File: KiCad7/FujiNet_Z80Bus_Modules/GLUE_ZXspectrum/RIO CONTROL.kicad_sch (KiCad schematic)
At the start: 8 parts, among them IC1 74HC32N, IC2 7404N, IC4 74HC08N, IC8 74HC32N, IC9 74HC08N, U1 74HC244N

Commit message: Reorganised the project again
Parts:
- renumbered U1 to U?
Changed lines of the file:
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@@
         )
         (path "/532c0392-800e-45cc-8170-6d32f2390e83/6a1fd481-1635-4a64-b244-c204161ad407/470a76e9-5ba5-4732-b286-3d7fc5c85df9"
-          (reference "IC8") (unit 2)
+          (reference "IC?") (unit 2)
         )
       )
@@
         )
         (path "/532c0392-800e-45cc-8170-6d32f2390e83/6a1fd481-1635-4a64-b244-c204161ad407/470a76e9-5ba5-4732-b286-3d7fc5c85df9"
-          (reference "IC5") (unit 2)
+          (reference "IC?") (unit 2)
         )
       )
@@
         )
         (path "/532c0392-800e-45cc-8170-6d32f2390e83/6a1fd481-1635-4a64-b244-c204161ad407/470a76e9-5ba5-4732-b286-3d7fc5c85df9"
-          (reference "#PWR064") (unit 1)
+          (reference "#PWR?") (unit 1)
         )
       )
@@
         )
         (path "/532c0392-800e-45cc-8170-6d32f2390e83/6a1fd481-1635-4a64-b244-c204161ad407/470a76e9-5ba5-4732-b286-3d7fc5c85df9"
-          (reference "IC11") (unit 5)
+          (reference "IC?") (unit 5)
         )
       )
@@
         )
         (path "/532c0392-800e-45cc-8170-6d32f2390e83/6a1fd481-1635-4a64-b244-c204161ad407/470a76e9-5ba5-4732-b286-3d7fc5c85df9"
-          (reference "IC7") (unit 1)
+          (reference "IC?") (unit 1)
         )
       )
@@
         )
         (path "/532c0392-800e-45cc-8170-6d32f2390e83/6a1fd481-1635-4a64-b244-c204161ad407/470a76e9-5ba5-4732-b286-3d7fc5c85df9"
-          (reference "IC8") (unit 1)
+          (reference "IC?") (unit 1)
         )
       )
@@
         )
         (path "/532c0392-800e-45cc-8170-6d32f2390e83/6a1fd481-1635-4a64-b244-c204161ad407/470a76e9-5ba5-4732-b286-3d7fc5c85df9"
-          (reference "IC8") (unit 3)
+          (reference "IC?") (unit 3)
         )
       )
@@
   (symbol (lib_id "power:GND") (at 214.63 152.4 0) (unit 1)
     (in_bom yes) (on_board yes) (dnp no) (fields_autoplaced)
-    (property "Reference" "#PWR065" (at 214.63 158.75 0)
+    (property "Reference" "#PWR?" (at 214.63 158.75 0)
       (effects (font (size 1.27 1.27)) hide)
     )
@@
       (project "FujiNet_Z80Bus_ReferenceDesign"
         (path "/532c0392-800e-45cc-8170-6d32f2390e83/6a1fd481-1635-4a64-b244-c204161ad407/470a76e9-5ba5-4732-b286-3d7fc5c85df9"
-          (reference "#PWR065") (unit 1)
+          (reference "#PWR?") (unit 1)
         )
       )
@@
         )
         (path "/532c0392-800e-45cc-8170-6d32f2390e83/6a1fd481-1635-4a64-b244-c204161ad407/470a76e9-5ba5-4732-b286-3d7fc5c85df9"
-          (reference "#PWR066") (unit 1)
+          (reference "#PWR?") (unit 1)
         )
       )
@@
         )
         (path "/532c0392-800e-45cc-8170-6d32f2390e83/6a1fd481-1635-4a64-b244-c204161ad407/470a76e9-5ba5-4732-b286-3d7fc5c85df9"
-          (reference "IC7") (unit 2)
+          (reference "IC?") (unit 2)
         )
       )
@@
         )
         (path "/532c0392-800e-45cc-8170-6d32f2390e83/6a1fd481-1635-4a64-b244-c204161ad407/470a76e9-5ba5-4732-b286-3d7fc5c85df9"
-          (reference "IC12") (unit 3)
+          (reference "IC?") (unit 3)
         )
       )
@@
         )
         (path "/532c0392-800e-45cc-8170-6d32f2390e83/6a1fd481-1635-4a64-b244-c204161ad407/470a76e9-5ba5-4732-b286-3d7fc5c85df9"
-          (reference "IC12") (unit 4)
+          (reference "IC?") (unit 4)
         )
       )
@@
         )
         (path "/532c0392-800e-45cc-8170-6d32f2390e83/6a1fd481-1635-4a64-b244-c204161ad407/470a76e9-5ba5-4732-b286-3d7fc5c85df9"
-          (reference "RN4") (unit 1)
+          (reference "RN?") (unit 1)
         )
       )
@@
         )
         (path "/532c0392-800e-45cc-8170-6d32f2390e83/6a1fd481-1635-4a64-b244-c204161ad407/470a76e9-5ba5-4732-b286-3d7fc5c85df9"
-          (reference "D14") (unit 1)
+          (reference "D?") (unit 1)
         )
       )
@@
   (symbol (lib_id "74xx:74HC244") (at 214.63 132.08 0) (unit 1)
     (in_bom yes) (on_board yes) (dnp no) (fields_autoplaced)
-    (property "Reference" "U1" (at 216.5859 113.03 0)
+    (property "Reference" "U?" (at 216.5859 113.03 0)
       (effects (font (size 1.27 1.27)) (justify left))
     )
@@
       (project "FujiNet_Z80Bus_ReferenceDesign"
         (path "/532c0392-800e-45cc-8170-6d32f2390e83/6a1fd481-1635-4a64-b244-c204161ad407/470a76e9-5ba5-4732-b286-3d7fc5c85df9"
+          (reference "U?") (unit 1)
+        )
+      )
+      (project "GLUE_ZXspectrum"
+        (path "/648e0b91-567a-4972-a379-57b42123c6d5/470a76e9-5ba5-4732-b286-3d7fc5c85df9"
           (reference "U1") (unit 1)
         )
       )
-      (project "GLUE_ZXspectrum"
-        (path "/648e0b91-567a-4972-a379-57b42123c6d5/470a76e9-5ba5-4732-b286-3d7fc5c85df9"
-          (reference "U1") (unit 1)
-        )
-      )
     )
   )
@@
         )
         (path "/532c0392-800e-45cc-8170-6d32f2390e83/6a1fd481-1635-4a64-b244-c204161ad407/470a76e9-5ba5-4732-b286-3d7fc5c85df9"
+          (reference "IC?") (unit 3)
+        )
+      )
+      (project "GLUE_ZXspectrum"
+        (path "/648e0b91-567a-4972-a379-57b42123c6d5/470a76e9-5ba5-4732-b286-3d7fc5c85df9"
           (reference "IC9") (unit 3)
         )
       )
-      (project "GLUE_ZXspectrum"
-        (path "/648e0b91-567a-4972-a379-57b42123c6d5/470a76e9-5ba5-4732-b286-3d7fc5c85df9"
-          (reference "IC9") (unit 3)
-        )
-      )
     )
   )
@@
         )
         (path "/532c0392-800e-45cc-8170-6d32f2390e83/6a1fd481-1635-4a64-b244-c204161ad407/470a76e9-5ba5-4732-b286-3d7fc5c85df9"
-          (reference "IC8") (unit 4)
-        )
-      )
+          (reference "IC?") (unit 4)
+        )
+      )

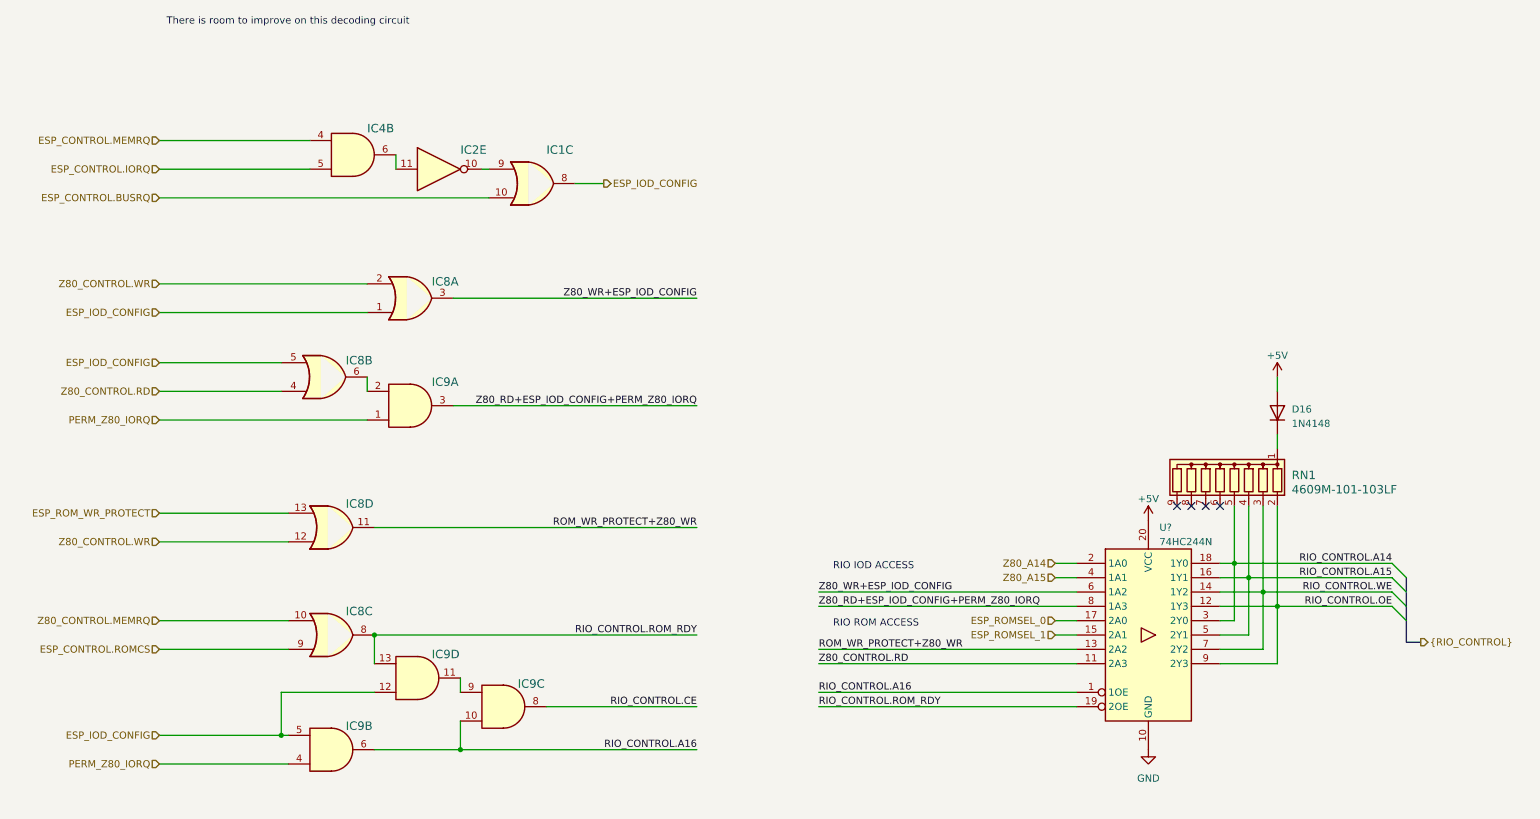
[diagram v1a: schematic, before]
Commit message: GLUE is broken again, logic gate annotation issue
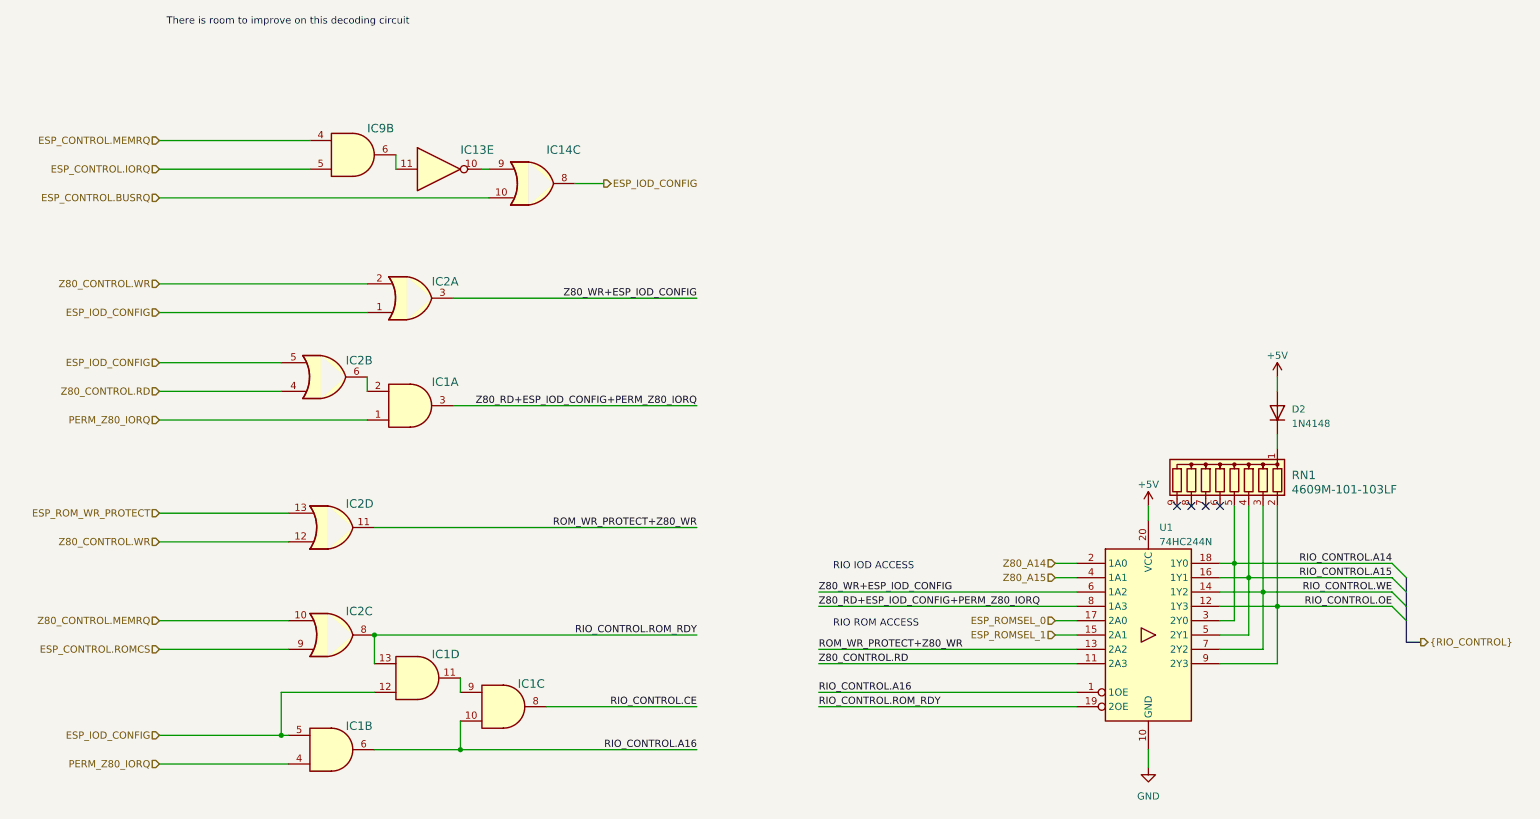
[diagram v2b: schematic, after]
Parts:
- gave numbers to parts that had none: 1
- renumbered D16 to D2, IC9 to IC1, IC2 to IC13, IC1 to IC14, IC8 to IC2, IC4 to IC9

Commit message: KiCad FIXED GLUE
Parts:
- renumbered IC13 to IC1, IC1 to IC4, IC2 to IC5, IC9 to IC6, IC1 to IC6, IC14 to IC7
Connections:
- net ESP_IOD_CONFIG: now also IC2.13; no longer IC2.5
- net RIO_CONTROL.A14: now also RN1.2 (R1); no longer RN1.5 (R4)
- net RIO_CONTROL.A15: now also RN1.3 (R2); no longer RN1.4 (R3)
- net RIO_CONTROL.OE: now also RN1.5 (R4); no longer RN1.2 (R1)
- net RIO_CONTROL.WE: now also RN1.4 (R3); no longer RN1.3 (R2)
- net Z80_CONTROL.RD: now also IC2.12; no longer IC2.4
- net at IC6.6: now also IC1.13; no longer IC1.11
- net at IC7.9: now also IC1.12; no longer IC1.10
- net at IC6.2: now also IC2.11; no longer IC2.6
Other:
- moved on the sheet: D2, RN1, U1

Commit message: KiCad Adapter Concept v2 pcb draft layout
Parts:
- renumbered D2 to D6, IC2 to IC5, IC5 to IC7
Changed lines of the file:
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@@
     (pin "7")
     (instances
-      (project "FujiNet_Z80Bus_ReferenceDesign"
-        (path "/532c0392-800e-45cc-8170-6d32f2390e83/6a1fd481-1635-4a64-b244-c204161ad407/470a76e9-5ba5-4732-b286-3d7fc5c85df9"
+      (project "ZXspectrum_Concept_v2.kicad_pro"
+        (path "/532c0392-800e-45cc-8170-6d32f2390e83/95233ba0-af33-48c6-a370-2e3f14ae4dcf/470a76e9-5ba5-4732-b286-3d7fc5c85df9"
           (reference "IC6") (unit 2)
         )
@@
     (pin "7")
     (instances
-      (project "FujiNet_Z80Bus_ReferenceDesign"
-        (path "/532c0392-800e-45cc-8170-6d32f2390e83/6a1fd481-1635-4a64-b244-c204161ad407/470a76e9-5ba5-4732-b286-3d7fc5c85df9"
+      (project "ZXspectrum_Concept_v2.kicad_pro"
+        (path "/532c0392-800e-45cc-8170-6d32f2390e83/95233ba0-af33-48c6-a370-2e3f14ae4dcf/470a76e9-5ba5-4732-b286-3d7fc5c85df9"
           (reference "IC4") (unit 2)
         )
@@
     (pin "1")
     (instances
-      (project "FujiNet_Z80Bus_ReferenceDesign"
-        (path "/532c0392-800e-45cc-8170-6d32f2390e83/6a1fd481-1635-4a64-b244-c204161ad407/470a76e9-5ba5-4732-b286-3d7fc5c85df9"
+      (project "ZXspectrum_Concept_v2.kicad_pro"
+        (path "/532c0392-800e-45cc-8170-6d32f2390e83/95233ba0-af33-48c6-a370-2e3f14ae4dcf/470a76e9-5ba5-4732-b286-3d7fc5c85df9"
           (reference "#PWR0104") (unit 1)
         )
@@
     (pin "7")
     (instances
-      (project "FujiNet_Z80Bus_ReferenceDesign"
-        (path "/532c0392-800e-45cc-8170-6d32f2390e83/6a1fd481-1635-4a64-b244-c204161ad407/470a76e9-5ba5-4732-b286-3d7fc5c85df9"
+      (project "ZXspectrum_Concept_v2.kicad_pro"
+        (path "/532c0392-800e-45cc-8170-6d32f2390e83/95233ba0-af33-48c6-a370-2e3f14ae4dcf/470a76e9-5ba5-4732-b286-3d7fc5c85df9"
           (reference "IC1") (unit 6)
         )
@@
     (pin "7")
     (instances
-      (project "FujiNet_Z80Bus_ReferenceDesign"
-        (path "/532c0392-800e-45cc-8170-6d32f2390e83/6a1fd481-1635-4a64-b244-c204161ad407/470a76e9-5ba5-4732-b286-3d7fc5c85df9"
+      (project "ZXspectrum_Concept_v2.kicad_pro"
+        (path "/532c0392-800e-45cc-8170-6d32f2390e83/95233ba0-af33-48c6-a370-2e3f14ae4dcf/470a76e9-5ba5-4732-b286-3d7fc5c85df9"
           (reference "IC5") (unit 1)
         )
@@
     (pin "7")
     (instances
-      (project "FujiNet_Z80Bus_ReferenceDesign"
-        (path "/532c0392-800e-45cc-8170-6d32f2390e83/6a1fd481-1635-4a64-b244-c204161ad407/470a76e9-5ba5-4732-b286-3d7fc5c85df9"
+      (project "ZXspectrum_Concept_v2.kicad_pro"
+        (path "/532c0392-800e-45cc-8170-6d32f2390e83/95233ba0-af33-48c6-a370-2e3f14ae4dcf/470a76e9-5ba5-4732-b286-3d7fc5c85df9"
           (reference "IC6") (unit 1)
         )
@@
     (pin "7")
     (instances
-      (project "FujiNet_Z80Bus_ReferenceDesign"
-        (path "/532c0392-800e-45cc-8170-6d32f2390e83/6a1fd481-1635-4a64-b244-c204161ad407/470a76e9-5ba5-4732-b286-3d7fc5c85df9"
+      (project "ZXspectrum_Concept_v2.kicad_pro"
+        (path "/532c0392-800e-45cc-8170-6d32f2390e83/95233ba0-af33-48c6-a370-2e3f14ae4dcf/470a76e9-5ba5-4732-b286-3d7fc5c85df9"
           (reference "IC4") (unit 3)
         )
@@
     (pin "1")
     (instances
-      (project "FujiNet_Z80Bus_ReferenceDesign"
-        (path "/532c0392-800e-45cc-8170-6d32f2390e83/6a1fd481-1635-4a64-b244-c204161ad407/470a76e9-5ba5-4732-b286-3d7fc5c85df9"
+      (project "ZXspectrum_Concept_v2.kicad_pro"
+        (path "/532c0392-800e-45cc-8170-6d32f2390e83/95233ba0-af33-48c6-a370-2e3f14ae4dcf/470a76e9-5ba5-4732-b286-3d7fc5c85df9"
           (reference "#PWR0105") (unit 1)
         )
@@
     (pin "1")
     (instances
-      (project "FujiNet_Z80Bus_ReferenceDesign"
-        (path "/532c0392-800e-45cc-8170-6d32f2390e83/6a1fd481-1635-4a64-b244-c204161ad407/470a76e9-5ba5-4732-b286-3d7fc5c85df9"
+      (project "ZXspectrum_Concept_v2.kicad_pro"
+        (path "/532c0392-800e-45cc-8170-6d32f2390e83/95233ba0-af33-48c6-a370-2e3f14ae4dcf/470a76e9-5ba5-4732-b286-3d7fc5c85df9"
           (reference "#PWR0103") (unit 1)
         )
@@
   (symbol (lib_id "74xx:74LS32") (at 68.58 86.36 0) (mirror x) (unit 4)
     (in_bom yes) (on_board yes) (dnp no)
-    (property "Reference" "IC2" (at 72.39 82.55 0)
+    (property "Reference" "IC5" (at 72.39 82.55 0)
       (effects (font (size 1.4986 1.4986)) (justify left bottom))
     )
@@
     (pin "7")
     (instances
-      (project "FujiNet_Z80Bus_ReferenceDesign"
-        (path "/532c0392-800e-45cc-8170-6d32f2390e83/6a1fd481-1635-4a64-b244-c204161ad407/470a76e9-5ba5-4732-b286-3d7fc5c85df9"
-          (reference "IC2") (unit 4)
+      (project "ZXspectrum_Concept_v2.kicad_pro"
+        (path "/532c0392-800e-45cc-8170-6d32f2390e83/95233ba0-af33-48c6-a370-2e3f14ae4dcf/470a76e9-5ba5-4732-b286-3d7fc5c85df9"
+          (reference "IC5") (unit 4)
         )
       )
@@
     (pin "7")
     (instances
-      (project "FujiNet_Z80Bus_ReferenceDesign"
-        (path "/532c0392-800e-45cc-8170-6d32f2390e83/6a1fd481-1635-4a64-b244-c204161ad407/470a76e9-5ba5-4732-b286-3d7fc5c85df9"
+      (project "ZXspectrum_Concept_v2.kicad_pro"
+        (path "/532c0392-800e-45cc-8170-6d32f2390e83/95233ba0-af33-48c6-a370-2e3f14ae4dcf/470a76e9-5ba5-4732-b286-3d7fc5c85df9"
           (reference "IC7") (unit 3)
         )
@@
   (symbol (lib_id "74xx:74LS32") (at 69.85 113.03 0) (mirror x) (unit 4)
     (in_bom yes) (on_board yes) (dnp no)
-    (property "Reference" "IC5" (at 72.39 107.95 0)
+    (property "Reference" "IC7" (at 72.39 107.95 0)
       (effects (font (size 1.4986 1.4986)) (justify left bottom))
     )
@@
     (pin "7")
     (instances
-      (project "FujiNet_Z80Bus_ReferenceDesign"
-        (path "/532c0392-800e-45cc-8170-6d32f2390e83/6a1fd481-1635-4a64-b244-c204161ad407/470a76e9-5ba5-4732-b286-3d7fc5c85df9"
-          (reference "IC5") (unit 4)
+      (project "ZXspectrum_Concept_v2.kicad_pro"
+        (path "/532c0392-800e-45cc-8170-6d32f2390e83/95233ba0-af33-48c6-a370-2e3f14ae4dcf/470a76e9-5ba5-4732-b286-3d7fc5c85df9"
+          (reference "IC7") (unit 4)
         )
       )
@@
     (pin "9")
     (instances
-      (project "FujiNet_Z80Bus_ReferenceDesign"
-        (path "/532c0392-800e-45cc-8170-6d32f2390e83/6a1fd481-1635-4a64-b244-c204161ad407/470a76e9-5ba5-4732-b286-3d7fc5c85df9"
+      (project "ZXspectrum_Concept_v2.kicad_pro"
+        (path "/532c0392-800e-45cc-8170-6d32f2390e83/95233ba0-af33-48c6-a370-2e3f14ae4dcf/470a76e9-5ba5-4732-b286-3d7fc5c85df9"
           (reference "RN1") (unit 1)
         )
@@
   (symbol (lib_id "Device:D") (at 226.06 33.02 270) (mirror x) (unit 1)
     (in_bom yes) (on_board yes) (dnp no) (fields_autoplaced)
-    (property "Reference" "D2" (at 228.6 32.385 90)
+    (property "Reference" "D6" (at 228.6 32.385 90)
       (effects (font (size 1.27 1.27)) (justify left))
     )
@@
     (pin "2")
     (instances
-      (project "FujiNet_Z80Bus_ReferenceDesign"
-        (path "/532c0392-800e-45cc-8170-6d32f2390e83/6a1fd481-1635-4a64-b244-c204161ad407/470a76e9-5ba5-4732-b286-3d7fc5c85df9"
-          (reference "D2") (unit 1)
+      (project "ZXspectrum_Concept_v2.kicad_pro"
+        (path "/532c0392-800e-45cc-8170-6d32f2390e83/95233ba0-af33-48c6-a370-2e3f14ae4dcf/470a76e9-5ba5-4732-b286-3d7fc5c85df9"
+          (reference "D6") (unit 1)
         )
       )
@@
     (pin "9")
     (instances
-      (project "FujiNet_Z80Bus_ReferenceDesign"
-        (path "/532c0392-800e-45cc-8170-6d32f2390e83/6a1fd481-1635-4a64-b244-c204161ad407/470a76e9-5ba5-4732-b286-3d7fc5c85df9"
+      (project "ZXspectrum_Concept_v2.kicad_pro"
+        (path "/532c0392-800e-45cc-8170-6d32f2390e83/95233ba0-af33-48c6-a370-2e3f14ae4dcf/470a76e9-5ba5-4732-b286-3d7fc5c85df9"
           (reference "U1") (unit 1)
         )
@@
     (pin "7")
     (instances
-      (project "FujiNet_Z80Bus_ReferenceDesign"
-        (path "/532c0392-800e-45cc-8170-6d32f2390e83/6a1fd481-1635-4a64-b244-c204161ad407/470a76e9-5ba5-4732-b286-3d7fc5c85df9"
+      (project "ZXspectrum_Concept_v2.kicad_pro"
+        (path "/532c0392-800e-45cc-8170-6d32f2390e83/95233ba0-af33-48c6-a370-2e3f14ae4dcf/470a76e9-5ba5-4732-b286-3d7fc5c85df9"
           (reference "IC5") (unit 3)
         )
@@
     (pin "7")
     (instances
-      (project "FujiNet_Z80Bus_ReferenceDesign"
-        (path "/532c0392-800e-45cc-8170-6d32f2390e83/6a1fd481-1635-4a64-b244-c204161ad407/470a76e9-5ba5-4732-b286-3d7fc5c85df9"
+      (project "ZXspectrum_Concept_v2.kicad_pro"
+        (path "/532c0392-800e-45cc-8170-6d32f2390e83/95233ba0-af33-48c6-a370-2e3f14ae4dcf/470a76e9-5ba5-4732-b286-3d7fc5c85df9"
           (reference "IC4") (unit 4)
         )
